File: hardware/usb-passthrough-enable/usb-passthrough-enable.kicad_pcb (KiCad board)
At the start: 2 copper layers, 71.1 x 35.6 mm, 12 parts, among them J1 Conn_02x04_Odd_Even, J2 USB_A, J3 USB_B, Q1 KSP43BU, U1 Omron_G3VM-61A1

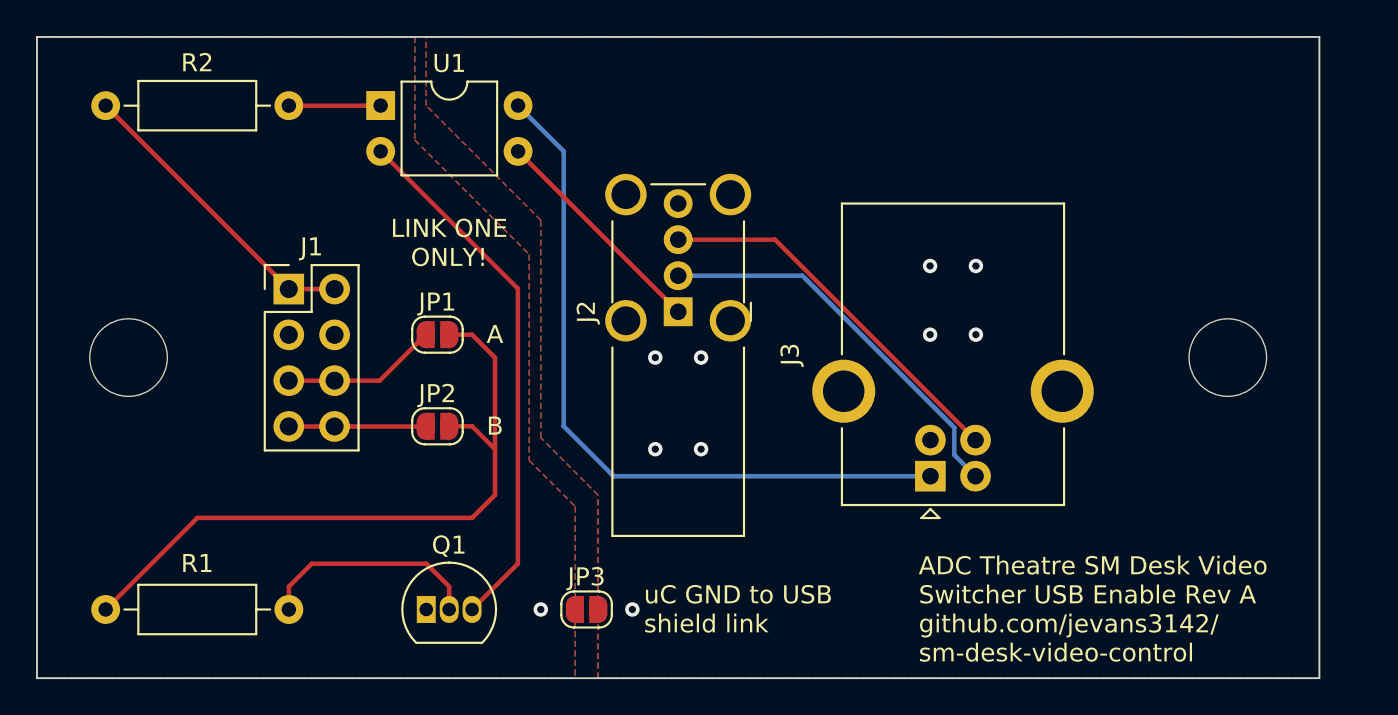
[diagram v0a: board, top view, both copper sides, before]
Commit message: Rev B USB switching PCB
Correct error in ground plane
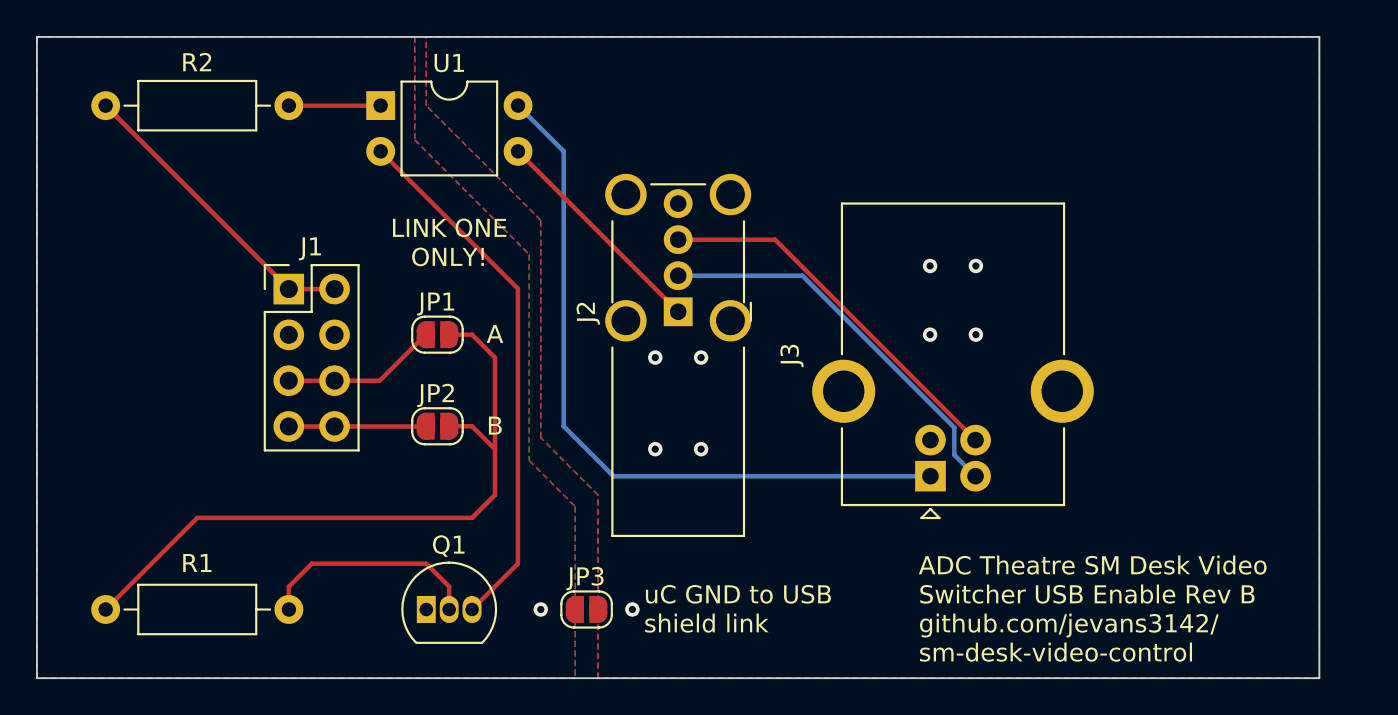
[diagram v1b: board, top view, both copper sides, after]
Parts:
- removed REF** (x2): MountingHole_4.3mm_M4, MountingHole:MountingHole_4.3mm_M4
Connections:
- J2 pad 4: Net-(J2-Pad4) -> GNDD
- J2 pad 5: Net-(J2-Pad4) -> GNDD
- J3 pad 4: Net-(J2-Pad4) -> GNDD
- J3 pad 5: Net-(J2-Pad4) -> GNDD
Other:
- board text added: "ADC Theatre SM Desk Video Switcher USB Enable Rev B github.com/jevans3142/ sm-desk-video-control"
- board text removed: "ADC Theatre SM Desk Video Switcher USB Enable Rev A github.com/jevans3142/ sm-desk-video-control"
